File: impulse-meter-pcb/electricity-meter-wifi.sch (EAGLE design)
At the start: 11 parts

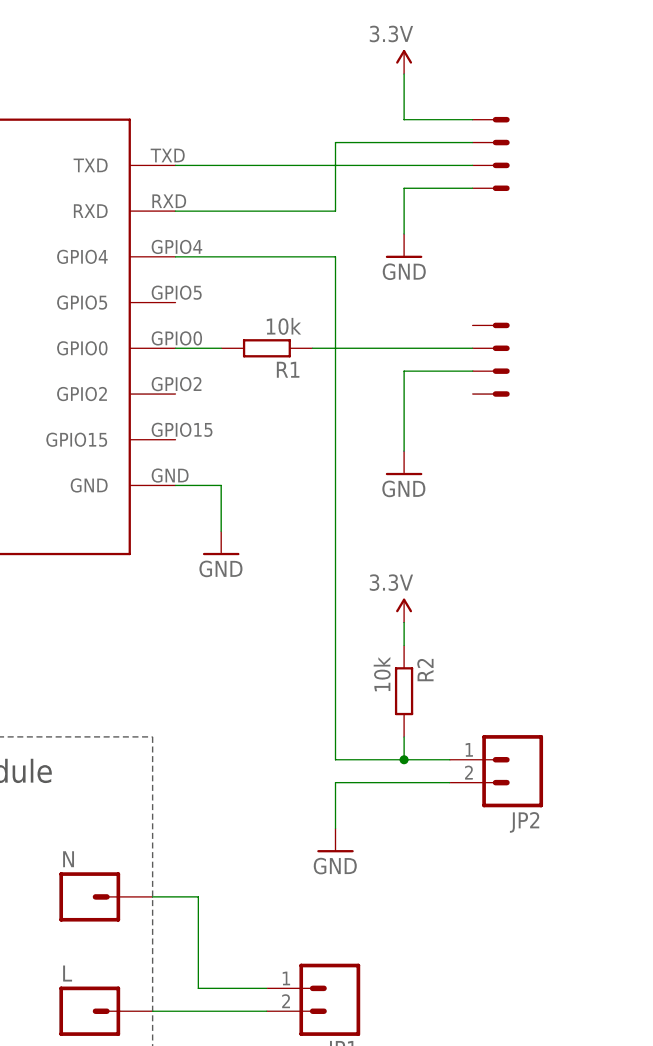
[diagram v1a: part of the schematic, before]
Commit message: added pull down on gpio 15
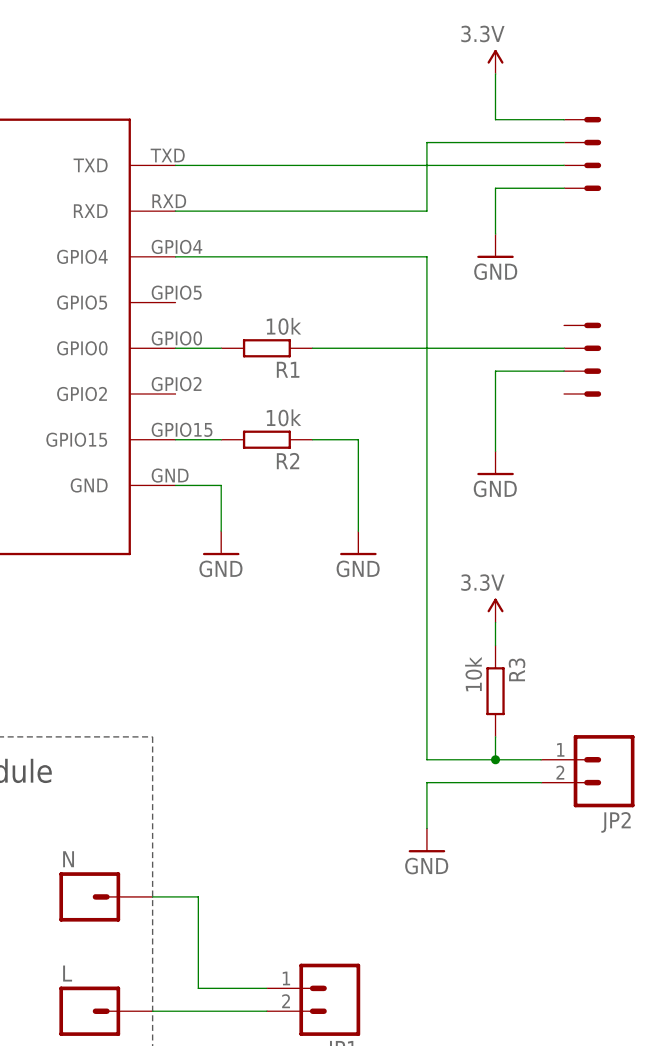
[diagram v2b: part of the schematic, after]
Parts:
- added R3: 10k, rcl:R-EU_R0805
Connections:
- new net N$7: ESP8266_ESP-07.GPIO15, R2.2
- net 3.3V: now also R3.1; no longer R2.1
- net GND: now also R2.1
- net N$3: now also R3.2; no longer R2.2
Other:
- moved on the sheet: JP2, R2
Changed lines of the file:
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@@
 <part name="U$1" library="con-pcb-slot" deviceset="CON-PCB-SLOT-0.05" device="MINIMAL"/>
 <part name="GND2" library="SparkFun-Aesthetics" deviceset="GND" device=""/>
+<part name="R3" library="rcl" deviceset="R-EU_" device="R0805" value="10k"/>
+<part name="SUPPLY3" library="SparkFun-Aesthetics" deviceset="3.3V" device=""/>
 <part name="R2" library="rcl" deviceset="R-EU_" device="R0805" value="10k"/>
-<part name="SUPPLY3" library="SparkFun-Aesthetics" deviceset="3.3V" device=""/>
+<part name="GND3" library="SparkFun-Aesthetics" deviceset="GND" device=""/>
 </parts>
 <sheets>
@@
 </plain>
 <instances>
-<instance part="GND4" gate="1" x="157.48" y="68.58" rot="MR0"/>
-<instance part="SUPPLY4" gate="G$1" x="157.48" y="88.9" rot="MR0"/>
-<instance part="GND5" gate="1" x="157.48" y="44.45"/>
+<instance part="GND4" gate="1" x="167.64" y="68.58" rot="MR0"/>
+<instance part="SUPPLY4" gate="G$1" x="167.64" y="88.9" rot="MR0"/>
+<instance part="GND5" gate="1" x="167.64" y="44.45"/>
 <instance part="R1" gate="G$1" x="142.24" y="58.42" rot="R180"/>
 <instance part="ESP8266_ESP-07" gate="G$1" x="106.68" y="53.34" smashed="yes">
@@
 <instance part="GND1" gate="1" x="76.2" y="-20.32"/>
 <instance part="JP1" gate="G$1" x="149.86" y="-12.7" rot="R180"/>
-<instance part="JP2" gate="G$1" x="170.18" y="12.7" rot="R180"/>
+<instance part="JP2" gate="G$1" x="180.34" y="12.7" rot="R180"/>
 <instance part="C1" gate="G$1" x="83.82" y="-7.62"/>
-<instance part="U$1" gate="G$1" x="165.1" y="76.2" smashed="yes" rot="MR180"/>
-<instance part="U$1" gate="G$2" x="165.1" y="78.74" smashed="yes" rot="MR180"/>
-<instance part="U$1" gate="G$3" x="165.1" y="81.28" smashed="yes" rot="MR180"/>
-<instance part="U$1" gate="G$4" x="165.1" y="83.82" smashed="yes" rot="MR180"/>
-<instance part="GND2" gate="1" x="149.86" y="2.54"/>
-<instance part="U$1" gate="G$5" x="165.1" y="60.96" smashed="yes"/>
-<instance part="U$1" gate="G$6" x="165.1" y="58.42" smashed="yes"/>
-<instance part="U$1" gate="G$7" x="165.1" y="55.88" smashed="yes"/>
-<instance part="U$1" gate="G$8" x="165.1" y="53.34" smashed="yes"/>
-<instance part="R2" gate="G$1" x="157.48" y="20.32" rot="R270"/>
-<instance part="SUPPLY3" gate="G$1" x="157.48" y="27.94" rot="MR0"/>
+<instance part="U$1" gate="G$1" x="175.26" y="76.2" smashed="yes" rot="MR180"/>
+<instance part="U$1" gate="G$2" x="175.26" y="78.74" smashed="yes" rot="MR180"/>
+<instance part="U$1" gate="G$3" x="175.26" y="81.28" smashed="yes" rot="MR180"/>
+<instance part="U$1" gate="G$4" x="175.26" y="83.82" smashed="yes" rot="MR180"/>
+<instance part="GND2" gate="1" x="160.02" y="2.54"/>
+<instance part="U$1" gate="G$5" x="175.26" y="60.96" smashed="yes"/>
+<instance part="U$1" gate="G$6" x="175.26" y="58.42" smashed="yes"/>
+<instance part="U$1" gate="G$7" x="175.26" y="55.88" smashed="yes"/>
+<instance part="U$1" gate="G$8" x="175.26" y="53.34" smashed="yes"/>
+<instance part="R3" gate="G$1" x="167.64" y="20.32" rot="R270"/>
+<instance part="SUPPLY3" gate="G$1" x="167.64" y="27.94" rot="MR0"/>
+<instance part="R2" gate="G$1" x="142.24" y="48.26" rot="R180"/>
+<instance part="GND3" gate="1" x="152.4" y="35.56"/>
 </instances>
 <busses>
@@
 <segment>
 <pinref part="GND2" gate="1" pin="GND"/>
-<wire x1="149.86" y1="10.16" x2="149.86" y2="5.08" width="0.1524" layer="91"/>
+<wire x1="160.02" y1="10.16" x2="160.02" y2="5.08" width="0.1524" layer="91"/>
 <pinref part="JP2" gate="G$1" pin="2"/>
-<wire x1="149.86" y1="10.16" x2="162.56" y2="10.16" width="0.1524" layer="91"/>
+<wire x1="160.02" y1="10.16" x2="172.72" y2="10.16" width="0.1524" layer="91"/>
 </segment>
 <segment>
 <pinref part="U$1" gate="G$7" pin="S"/>
 <pinref part="GND5" gate="1" pin="GND"/>
-<wire x1="165.1" y1="55.88" x2="157.48" y2="55.88" width="0.1524" layer="91"/>
-<wire x1="157.48" y1="55.88" x2="157.48" y2="46.99" width="0.1524" layer="91"/>
+<wire x1="175.26" y1="55.88" x2="167.64" y2="55.88" width="0.1524" layer="91"/>
+<wire x1="167.64" y1="55.88" x2="167.64" y2="46.99" width="0.1524" layer="91"/>
 </segment>
 <segment>
 <pinref part="U$1" gate="G$1" pin="S"/>
-<wire x1="165.1" y1="76.2" x2="157.48" y2="76.2" width="0.1524" layer="91"/>
+<wire x1="175.26" y1="76.2" x2="167.64" y2="76.2" width="0.1524" layer="91"/>
 <pinref part="GND4" gate="1" pin="GND"/>
-<wire x1="157.48" y1="76.2" x2="157.48" y2="71.12" width="0.1524" layer="91"/>
+<wire x1="167.64" y1="76.2" x2="167.64" y2="71.12" width="0.1524" layer="91"/>
+</segment>
+<segment>
+<pinref part="GND3" gate="1" pin="GND"/>
+<wire x1="152.4" y1="38.1" x2="152.4" y2="48.26" width="0.1524" layer="91"/>
+<pinref part="R2" gate="G$1" pin="1"/>
+<wire x1="152.4" y1="48.26" x2="147.32" y2="48.26" width="0.1524" layer="91"/>
 </segment>
 </net>
@@
 <segment>
 <pinref part="U$1" gate="G$4" pin="S"/>
-<wire x1="157.48" y1="83.82" x2="165.1" y2="83.82" width="0.1524" layer="91"/>
+<wire x1="167.64" y1="83.82" x2="175.26" y2="83.82" width="0.1524" layer="91"/>
 <pinref part="SUPPLY4" gate="G$1" pin="3.3V"/>
-<wire x1="157.48" y1="83.82" x2="157.48" y2="88.9" width="0.1524" layer="91"/>
-</segment>
-<segment>
-<pinref part="R2" gate="G$1" pin="1"/>
+<wire x1="167.64" y1="83.82" x2="167.64" y2="88.9" width="0.1524" layer="91"/>
+</segment>
+<segment>
+<pinref part="R3" gate="G$1" pin="1"/>
 <pinref part="SUPPLY3" gate="G$1" pin="3.3V"/>
-<wire x1="157.48" y1="25.4" x2="157.48" y2="27.94" width="0.1524" layer="91"/>
+<wire x1="167.64" y1="25.4" x2="167.64" y2="27.94" width="0.1524" layer="91"/>
 </segment>
 </net>
@@
 <pinref part="R1" gate="G$1" pin="1"/>
 <pinref part="U$1" gate="G$6" pin="S"/>
-<wire x1="147.32" y1="58.42" x2="165.1" y2="58.42" width="0.1524" layer="91"/>
+<wire x1="147.32" y1="58.42" x2="175.26" y2="58.42" width="0.1524" layer="91"/>
 </segment>
 </net>
@@
 <pinref part="ESP8266_ESP-07" gate="G$1" pin="TXD"/>
 <pinref part="U$1" gate="G$2" pin="S"/>
-<wire x1="132.08" y1="78.74" x2="165.1" y2="78.74" width="0.1524" layer="91"/>
+<wire x1="132.08" y1="78.74" x2="175.26" y2="78.74" width="0.1524" layer="91"/>
 </segment>
 </net>
@@
 <segment>
 <pinref part="ESP8266_ESP-07" gate="G$1" pin="RXD"/>
-<wire x1="132.08" y1="73.66" x2="149.86" y2="73.66" width="0.1524" layer="91"/>
-<wire x1="149.86" y1="73.66" x2="149.86" y2="81.28" width="0.1524" layer="91"/>
+<wire x1="132.08" y1="73.66" x2="160.02" y2="73.66" width="0.1524" layer="91"/>
+<wire x1="160.02" y1="73.66" x2="160.02" y2="81.28" width="0.1524" layer="91"/>
 <pinref part="U$1" gate="G$3" pin="S"/>
-<wire x1="149.86" y1="81.28" x2="165.1" y2="81.28" width="0.1524" layer="91"/>
+<wire x1="160.02" y1="81.28" x2="175.26" y2="81.28" width="0.1524" layer="91"/>
 </segment>
 </net>
@@
 <segment>
 <pinref part="JP2" gate="G$1" pin="1"/>
-<wire x1="162.56" y1="12.7" x2="157.48" y2="12.7" width="0.1524" layer="91"/>
+<wire x1="172.72" y1="12.7" x2="167.64" y2="12.7" width="0.1524" layer="91"/>
+<pinref part="R3" gate="G$1" pin="2"/>
+<wire x1="167.64" y1="15.24" x2="167.64" y2="12.7" width="0.1524" layer="91"/>
+<junction x="167.64" y="12.7"/>
+<wire x1="167.64" y1="12.7" x2="160.02" y2="12.7" width="0.1524" layer="91"/>
+<pinref part="ESP8266_ESP-07" gate="G$1" pin="GPIO4"/>
+<wire x1="132.08" y1="68.58" x2="160.02" y2="68.58" width="0.1524" layer="91"/>
+<wire x1="160.02" y1="68.58" x2="160.02" y2="12.7" width="0.1524" layer="91"/>
+</segment>
+</net>
+<net name="N$7" class="0">
+<segment>
 <pinref part="R2" gate="G$1" pin="2"/>
-<wire x1="157.48" y1="15.24" x2="157.48" y2="12.7" width="0.1524" layer="91"/>
-<junction x="157.48" y="12.7"/>
-<wire x1="157.48" y1="12.7" x2="149.86" y2="12.7" width="0.1524" layer="91"/>
-<pinref part="ESP8266_ESP-07" gate="G$1" pin="GPIO4"/>
-<wire x1="132.08" y1="68.58" x2="149.86" y2="68.58" width="0.1524" layer="91"/>
-<wire x1="149.86" y1="68.58" x2="149.86" y2="12.7" width="0.1524" layer="91"/>
-</segment>
-</net>
+<pinref part="ESP8266_ESP-07" gate="G$1" pin="GPIO15"/>
+<wire x1="137.16" y1="48.26" x2="132.08" y2="48.26" width="0.1524" layer="91"/>
+</segment>
+</net>

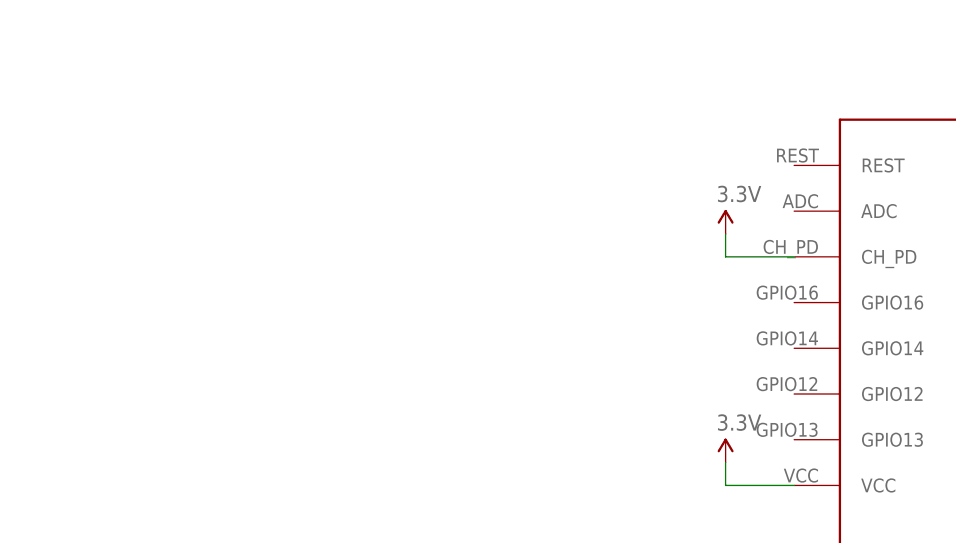
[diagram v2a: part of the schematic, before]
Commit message: pcb: v.1.3.1
added voltage supervisor MCP1316MT-29ME/OT
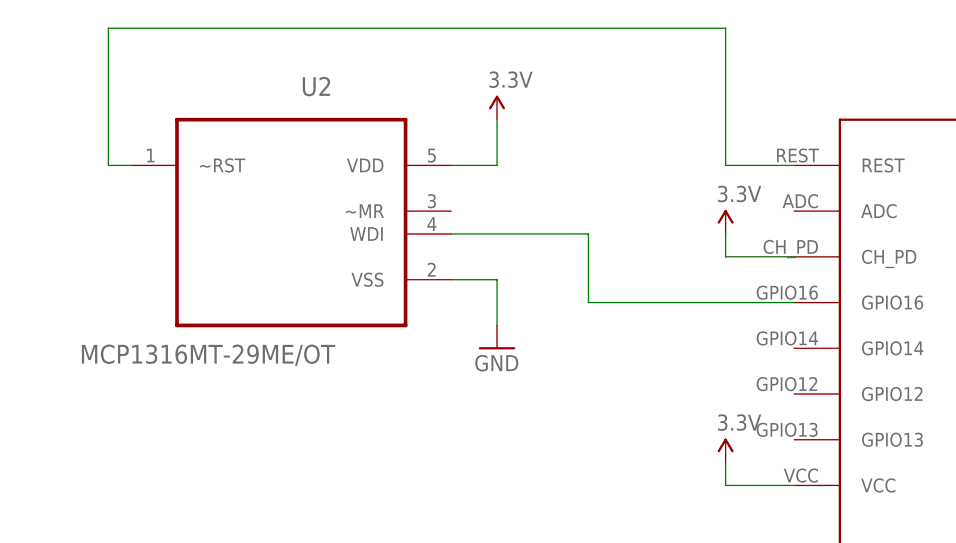
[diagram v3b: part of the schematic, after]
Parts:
- added U2: MCP1316MT-29ME/OT, Microchip_By_element14_Batch_1:MCP1316T-29LE/OT
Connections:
- new net N$8: ESP8266_ESP-07.REST, U2.~RST
- new net N$9: ESP8266_ESP-07.GPIO16, U2.WDI
- net 3.3V: now also U2.VDD
- net GND: now also U2.VSS
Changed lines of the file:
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@@
 <part name="R2" library="rcl" deviceset="R-EU_" device="R0805" value="10k"/>
 <part name="GND3" library="SparkFun-Aesthetics" deviceset="GND" device=""/>
+<part name="U2" library="Microchip_By_element14_Batch_1" deviceset="MCP1316T-29LE/OT" device="" value="MCP1316MT-29ME/OT"/>
+<part name="SUPPLY5" library="SparkFun-Aesthetics" deviceset="3.3V" device=""/>
+<part name="GND6" library="SparkFun-Aesthetics" deviceset="GND" device=""/>
 </parts>
 <sheets>
@@
 <instance part="R2" gate="G$1" x="142.24" y="48.26" rot="R180"/>
 <instance part="GND3" gate="1" x="152.4" y="35.56"/>
+<instance part="U2" gate="A" x="30.48" y="76.2" rot="MR0"/>
+<instance part="SUPPLY5" gate="G$1" x="53.34" y="83.82"/>
+<instance part="GND6" gate="1" x="53.34" y="58.42"/>
 </instances>
 <busses>
@@
 <wire x1="152.4" y1="48.26" x2="147.32" y2="48.26" width="0.1524" layer="91"/>
 </segment>
+<segment>
+<pinref part="U2" gate="A" pin="VSS"/>
+<pinref part="GND6" gate="1" pin="GND"/>
+<wire x1="48.26" y1="66.04" x2="53.34" y2="66.04" width="0.1524" layer="91"/>
+<wire x1="53.34" y1="66.04" x2="53.34" y2="60.96" width="0.1524" layer="91"/>
+</segment>
 </net>
 <net name="3.3V" class="0">
@@
 <pinref part="SUPPLY3" gate="G$1" pin="3.3V"/>
 <wire x1="167.64" y1="25.4" x2="167.64" y2="27.94" width="0.1524" layer="91"/>
+</segment>
+<segment>
+<pinref part="U2" gate="A" pin="VDD"/>
+<pinref part="SUPPLY5" gate="G$1" pin="3.3V"/>
+<wire x1="48.26" y1="78.74" x2="53.34" y2="78.74" width="0.1524" layer="91"/>
+<wire x1="53.34" y1="78.74" x2="53.34" y2="83.82" width="0.1524" layer="91"/>
 </segment>
 </net>
@@
 </segment>
 </net>
+<net name="N$8" class="0">
+<segment>
+<pinref part="U2" gate="A" pin="~RST"/>
+<wire x1="12.7" y1="78.74" x2="10.16" y2="78.74" width="0.1524" layer="91"/>
+<wire x1="10.16" y1="78.74" x2="10.16" y2="93.98" width="0.1524" layer="91"/>
+<wire x1="10.16" y1="93.98" x2="78.74" y2="93.98" width="0.1524" layer="91"/>
+<wire x1="78.74" y1="93.98" x2="78.74" y2="78.74" width="0.1524" layer="91"/>
+<pinref part="ESP8266_ESP-07" gate="G$1" pin="REST"/>
+<wire x1="78.74" y1="78.74" x2="86.36" y2="78.74" width="0.1524" layer="91"/>
+</segment>
+</net>
+<net name="N$9" class="0">
+<segment>
+<pinref part="ESP8266_ESP-07" gate="G$1" pin="GPIO16"/>
+<wire x1="86.36" y1="63.5" x2="63.5" y2="63.5" width="0.1524" layer="91"/>
+<wire x1="63.5" y1="63.5" x2="63.5" y2="71.12" width="0.1524" layer="91"/>
+<pinref part="U2" gate="A" pin="WDI"/>
+<wire x1="63.5" y1="71.12" x2="48.26" y2="71.12" width="0.1524" layer="91"/>
+</segment>
+</net>

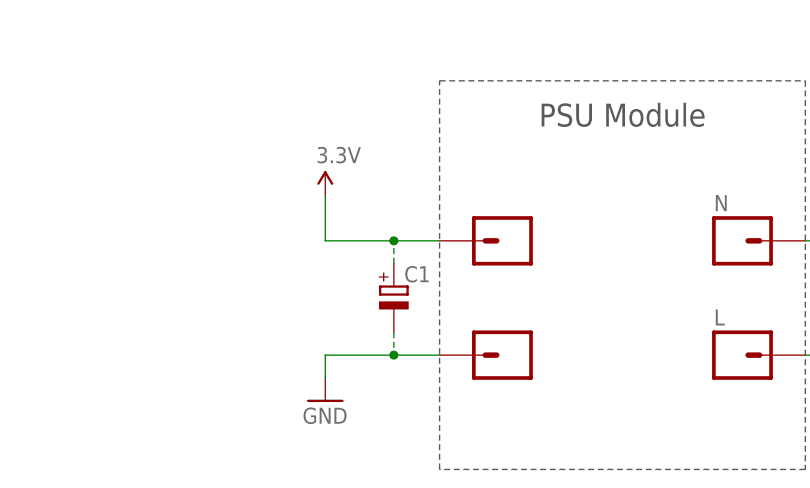
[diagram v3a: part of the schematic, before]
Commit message: pcb v1.3.4
added PE hole
rotated c1
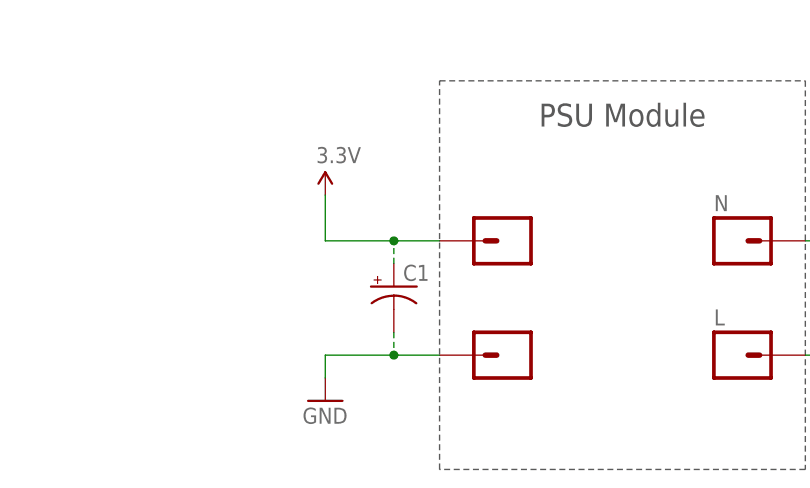
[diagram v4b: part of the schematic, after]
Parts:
- C1: device rcl:CPOL-EUG -> SparkFun-Capacitors:CAP_POLD
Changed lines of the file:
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@@
 <part name="JP1" library="SparkFun (old)" deviceset="M02" device="PTH3_5MM"/>
 <part name="JP2" library="SparkFun (old)" deviceset="M02" device="PTH3_5MM"/>
-<part name="C1" library="rcl" deviceset="CPOL-EU" device="G"/>
+<part name="C1" library="SparkFun-Capacitors" deviceset="CAP_POL" device="D"/>
 <part name="U$1" library="con-pcb-slot" deviceset="CON-PCB-SLOT-0.05" device="MINIMAL"/>
 <part name="GND2" library="SparkFun-Aesthetics" deviceset="GND" device=""/>
